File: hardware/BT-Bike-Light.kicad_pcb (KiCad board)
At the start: 4 copper layers, 35.1 x 27.5 mm, 36 parts, among them J101 USB_C_Charge_Port, J102 Conn_ARM_SWD_TagConnect_TC203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, Q101 DMN3731U-7, SW102 Button, U101 BT840, U102 nPM1300, U103 FEM11-F09, U105 TPS92201

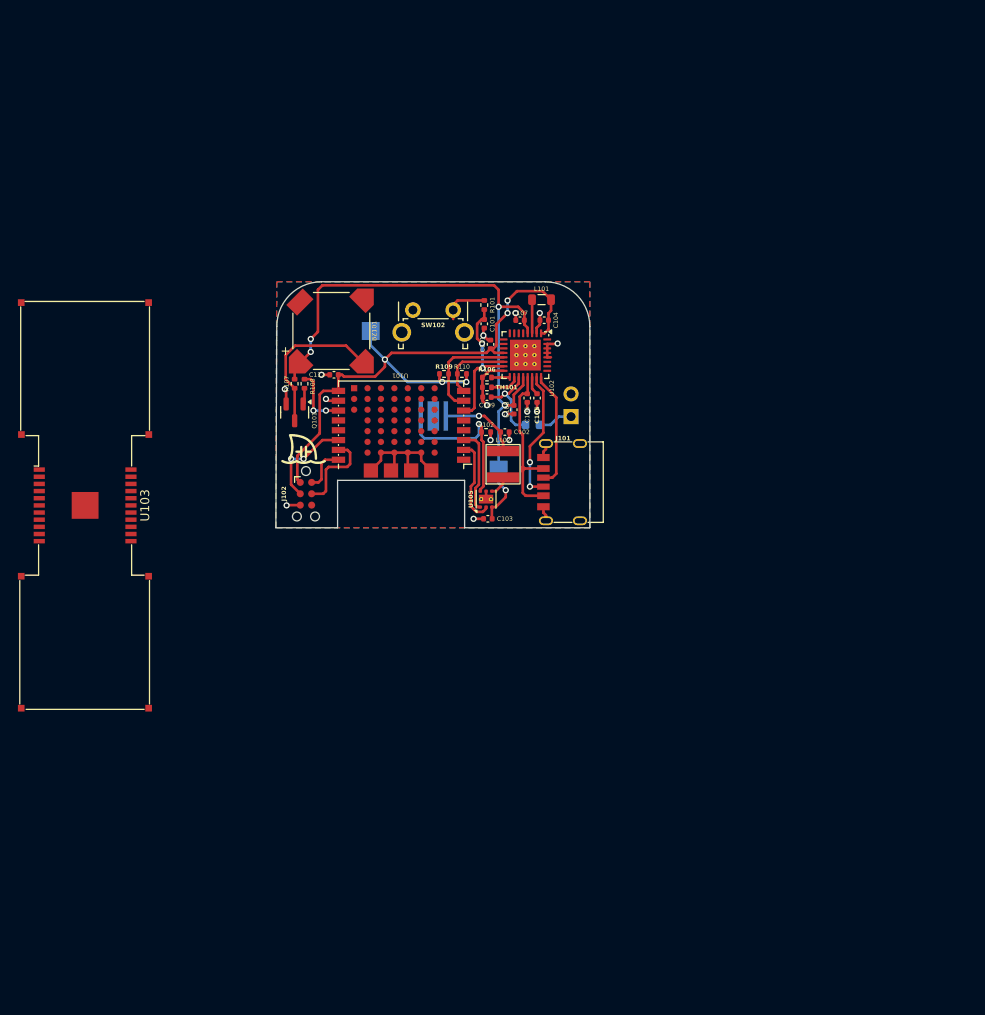
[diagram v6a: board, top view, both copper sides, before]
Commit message: New battery connector and board outline
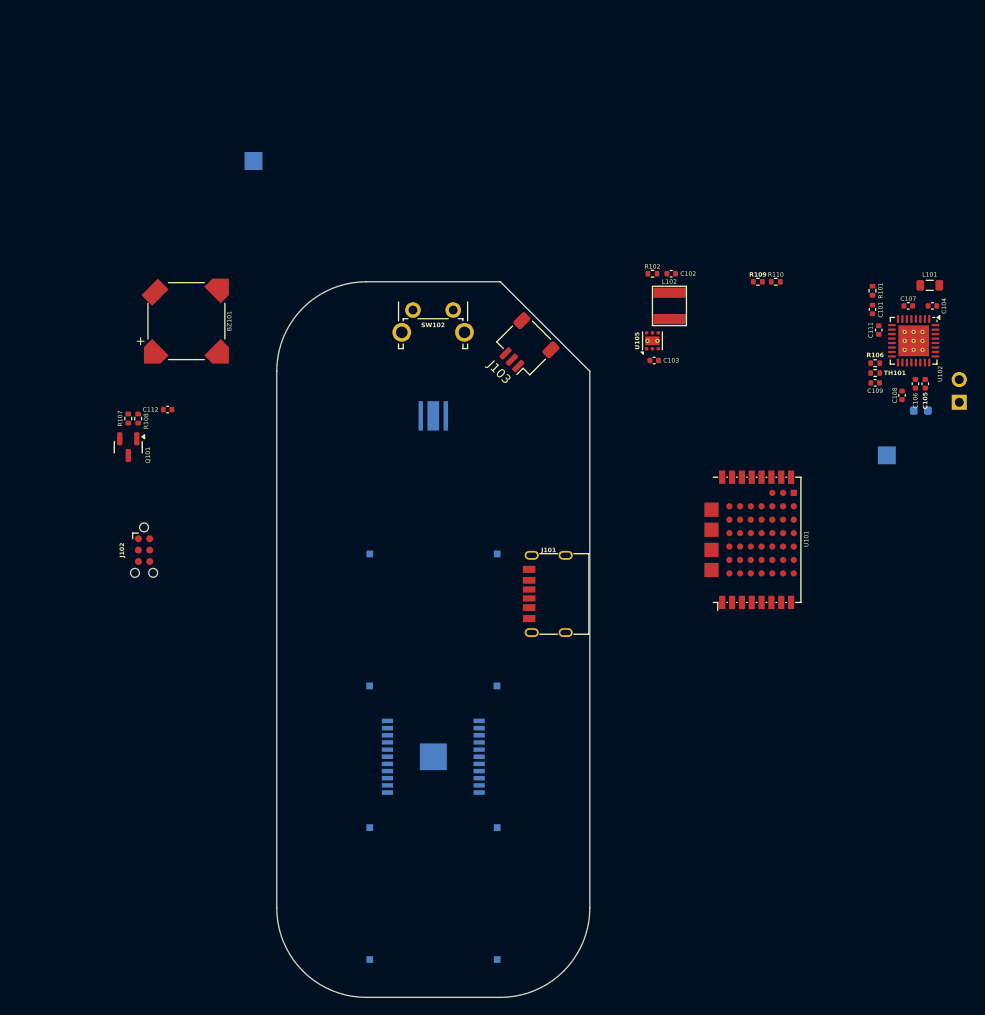
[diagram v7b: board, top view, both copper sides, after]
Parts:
- added J103: Conn_01x03, Connector_JST:JST_SH_SM03B-SRSS-TB_1x03-1MP_P1.00mm_Horizontal, F.Cu at (152.7, 87.3)
- G***, U103: moved to B.Cu
- moved U103 48.0 mm to (142.5, 133.1)
- moved BT101 43.4 mm to (201.3, 93.5)
- moved C101 43.4 mm to (191.6, 83.1)
- moved C109 43.4 mm to (191.9, 91.3)
- moved R106 43.4 mm to (191.9, 89.1)
- moved C104 43.4 mm to (198.3, 82.7)
- moved C105 43.4 mm to (197.5, 91.4)
- moved C106 43.4 mm to (196.4, 91.4)
- moved C107 43.4 mm to (195.6, 82.7)
- moved C108 43.4 mm to (194.9, 92.7)
- moved C111 43.4 mm to (192.3, 85.4)
- moved F101 43.4 mm to (197.0, 94.4)
- moved L101 43.4 mm to (198.0, 80.4)
- moved R101 43.4 mm to (191.6, 81.0)
- moved TH101 43.4 mm to (191.9, 90.2)
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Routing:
- net VSYS: track 69.4 -> 0.00 mm, vias 5 -> 0
- net +1V8: track 68.0 -> 0.00 mm, vias 5 -> 0
- net GND: track 43.9 -> 0.00 mm, vias 15 -> 0
- net VBUS: track 19.2 -> 0.00 mm
- net Net-(BZ101--): track 18.0 -> 0.00 mm
- net Net-(D101-K): track 18.0 -> 0.00 mm, vias 1 -> 0
- net /BTN: track 16.2 -> 0.00 mm, vias 2 -> 0
- net Net-(J101-CC1): track 14.7 -> 0.00 mm, vias 2 -> 0
- net Net-(J101-CC2): track 13.1 -> 0.00 mm
- net /SDA: track 12.0 -> 0.00 mm
- net /nRST: track 10.5 -> 0.00 mm, vias 2 -> 0
- net /SWCLK: track 9.78 -> 0.00 mm
- net /LED_EN: track 9.78 -> 0.00 mm
- net /VBAT_FUSE: track 9.54 -> 0.00 mm, vias 1 -> 0
- net /LED_PWM: track 9.50 -> 0.00 mm
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- removed copper zone on B.Cu, net GND
- removed copper zone on F.Cu, net GND
- removed copper zone on In1.Cu, net GND
- removed copper zone on In2.Cu, net GND
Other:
- board size 35.1 x 27.5 mm -> 35 x 80 mm

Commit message: Increase passive component sizes
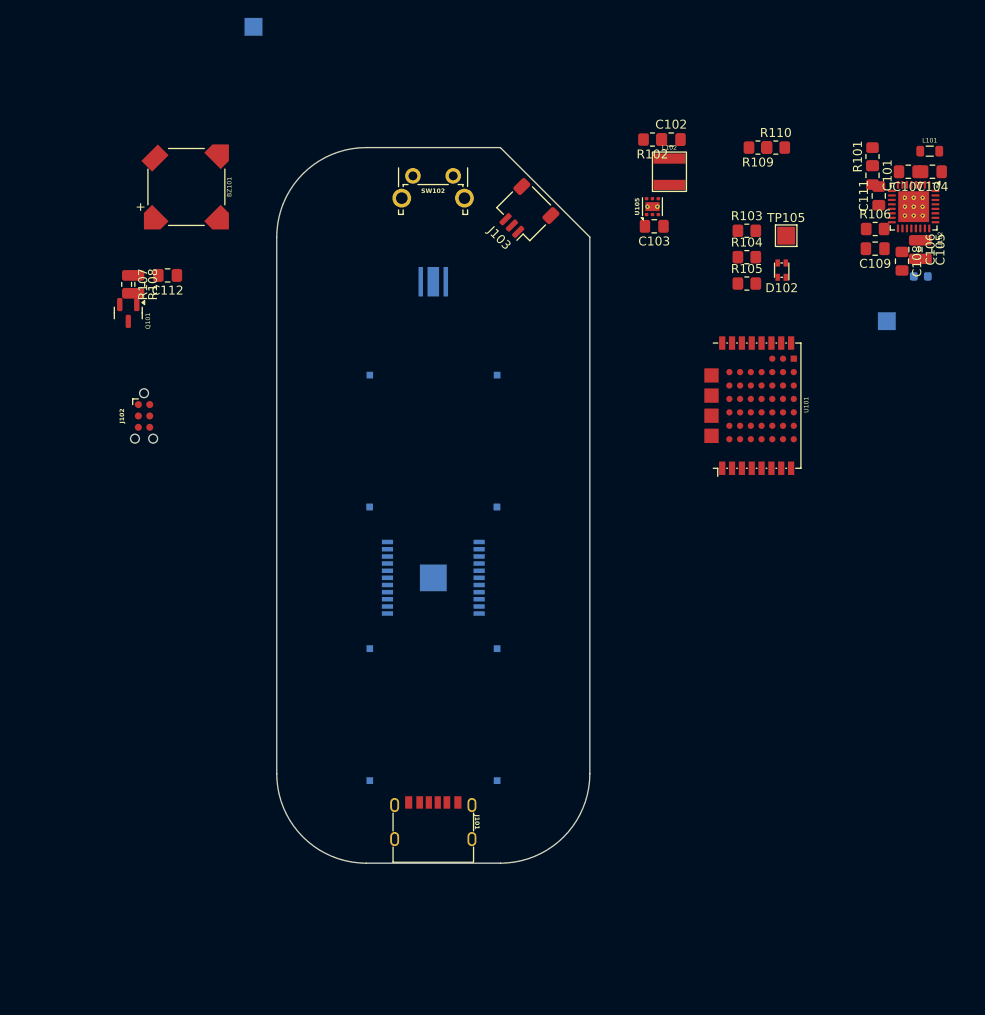
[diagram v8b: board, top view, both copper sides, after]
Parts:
- removed BT101: 18650, Connector_PinHeader_2.54mm:PinHeader_1x02_P2.54mm_Vertical
- removed TH101: 10K, Resistor_SMD:R_0402_1005Metric
- added D102: CHRG_LED, Generic_Custom:LED_0606, F.Cu at (181.4, 78.7)
- added R103: 110, Resistor_SMD:R_0805_2012Metric_Pad1.20x1.40mm_HandSolder, F.Cu at (177.6, 74.3)
- added R104: 110, Resistor_SMD:R_0805_2012Metric_Pad1.20x1.40mm_HandSolder, F.Cu at (177.6, 77.2)
- added R105: 110, Resistor_SMD:R_0805_2012Metric_Pad1.20x1.40mm_HandSolder, F.Cu at (177.6, 80.2)
- added TP105: 1V8, TestPoint:TestPoint_Pad_2.0x2.0mm, F.Cu at (181.9, 74.8)
- C101, C102, C103, C104, C105, C106, C107, C108, C109, C111, C112: footprint Capacitor_SMD:C_0402_1005Metric -> Capacitor_SMD:C_0805_2012Metric_Pad1.18x1.45mm_HandSolder
- J103: value Conn_01x03 -> BATT
- R101, R102, R106, R107, R108, R109, R110: footprint Resistor_SMD:R_0402_1005Metric -> Resistor_SMD:R_0805_2012Metric_Pad1.20x1.40mm_HandSolder
- moved J101 26.0 mm to (142.5, 138.5), turned to 0 degrees
- moved U103 20.0 mm to (142.5, 113.1)
- moved BZ101 15.0 mm to (114.9, 69.4)
- moved C101 15.0 mm to (191.6, 68.1)
- moved C102 15.0 mm to (169.1, 64.1)
- moved C103 15.0 mm to (167.2, 73.8)
- moved C104 15.0 mm to (198.3, 67.7)
- moved C105 15.0 mm to (197.5, 76.4)
- moved C106 15.0 mm to (196.4, 76.4)
- moved C107 15.0 mm to (195.6, 67.7)
- moved C108 15.0 mm to (194.9, 77.7)
- moved C109 15.0 mm to (191.9, 76.3)
- moved C111 15.0 mm to (192.3, 70.4)
- moved C112 15.0 mm to (112.8, 79.3)
- moved D101 15.0 mm to (142.5, 80.0)
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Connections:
- C109 pad 1: /VBAT_FUSE -> +BATT
- F101 pad 1: +BATT -> Net-(J103-Pin_1)
- F101 pad 2: /VBAT_FUSE -> +BATT
- J103 pad 1: unconnected-(J103-Pin_1-Pad1) -> Net-(J103-Pin_1)
- J103 pad 2: unconnected-(J103-Pin_2-Pad2) -> /BATT_NTC
- J103 pad 3: unconnected-(J103-Pin_3-Pad3) -> GND
- U102 pad 18: Net-(U102-NTC) -> /BATT_NTC
- U102 pad 19: /VBAT_FUSE -> +BATT
